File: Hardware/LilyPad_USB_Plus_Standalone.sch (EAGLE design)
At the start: 72 parts, among them J1 SEWTAP_LONG-2SIDE, J10 SEWTAP_LONG-2SIDE, J11 SEWTAP_LONG-2SIDE, J12 SEWTAP_LONG-2SIDE, J13 SEWTAP_LONG-2SIDE, J14 SEWTAP_LONG-2SIDE, J15 AMP FCI 10103594-0001LF, J2 SEWTAP_LONG-2SIDE, J3 SEWTAP_LONG-2SIDE, J4 SEWTAP_LONG-2SIDE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

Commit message: Cleaned up some things
Ready for proto review
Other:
- note added: "Revised by: Elias Santistevan"
- note added: "v01"
- note removed: "v10"
- moved on the sheet: TP5, TP6
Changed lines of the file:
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@@
 <text x="220.98" y="151.13" size="1.27" layer="97">MIC5219 BYPASS</text>
 <text x="171.45" y="11.43" size="2.54" layer="94">Marshall Taylor</text>
-<text x="238.252" y="7.112" size="2.54" layer="94">v10</text>
+<text x="238.252" y="7.112" size="2.54" layer="94">v01</text>
 <text x="149.86" y="38.1" size="2.54" layer="94">LilyPad concept and shapes by:
 L. Buechley and N. Seidle</text>
@@
 <text x="5.08" y="5.08" size="2.032" layer="97" font="vector">Supply 5.0V from USB, or
 3.3-4.2V on battery connector.</text>
+<text x="148.844" y="7.112" size="2.54" layer="94">Revised by: Elias Santistevan</text>
 </plain>
 <instances>
@@
 <instance part="GND26" gate="1" x="172.72" y="144.78"/>
 <instance part="U$1" gate="G$1" x="220.98" y="38.1"/>
-<instance part="LOGO6" gate="G$1" x="233.68" y="53.34"/>
+<instance part="LOGO6" gate="G$1" x="233.68" y="55.88"/>
 <instance part="D10" gate="G1" x="157.48" y="157.48" smashed="yes">
 <attribute name="NAME" x="149.86" y="162.8775" size="1.778" layer="95" font="vector"/>
 <attribute name="VALUE" x="139.7" y="152.0825" size="1.778" layer="95" font="vector" align="top-left"/>
 </instance>
-<instance part="TP5" gate="G$1" x="167.64" y="58.42" rot="R180"/>
-<instance part="TP6" gate="G$1" x="167.64" y="68.58" rot="R180"/>
-<instance part="GND28" gate="1" x="172.72" y="53.34"/>
-<instance part="P+9" gate="G$1" x="172.72" y="73.66"/>
+<instance part="TP5" gate="G$1" x="170.18" y="58.42" rot="R180"/>
+<instance part="TP6" gate="G$1" x="170.18" y="68.58" rot="R180"/>
+<instance part="GND28" gate="1" x="175.26" y="53.34"/>
+<instance part="P+9" gate="G$1" x="175.26" y="73.66"/>
 <instance part="TP7" gate="G$1" x="93.98" y="48.26" rot="R90"/>
 <instance part="TP8" gate="G$1" x="109.22" y="22.86"/>
-<instance part="LOGO1" gate="G$1" x="88.9" y="-2.54"/>
+<instance part="LOGO1" gate="G$1" x="90.932" y="-2.032"/>
 </instances>
 <busses>
@@
 <pinref part="TP5" gate="G$1" pin="1"/>
 <pinref part="GND28" gate="1" pin="GND"/>
-<wire x1="167.64" y1="58.42" x2="172.72" y2="58.42" width="0.1524" layer="91"/>
-<wire x1="172.72" y1="58.42" x2="172.72" y2="55.88" width="0.1524" layer="91"/>
+<wire x1="170.18" y1="58.42" x2="175.26" y2="58.42" width="0.1524" layer="91"/>
+<wire x1="175.26" y1="58.42" x2="175.26" y2="55.88" width="0.1524" layer="91"/>
 </segment>
 </net>
@@
 <pinref part="TP6" gate="G$1" pin="1"/>
 <pinref part="P+9" gate="G$1" pin="3.3V"/>
-<wire x1="167.64" y1="68.58" x2="172.72" y2="68.58" width="0.1524" layer="91"/>
-<wire x1="172.72" y1="68.58" x2="172.72" y2="73.66" width="0.1524" layer="91"/>
-</segment>
-</net>
+<wire x1="170.18" y1="68.58" x2="175.26" y2="68.58" width="0.1524" layer="91"/>
+<wire x1="175.26" y1="68.58" x2="175.26" y2="73.66" width="0.1524" layer="91"/>
+</segment>
+</net>

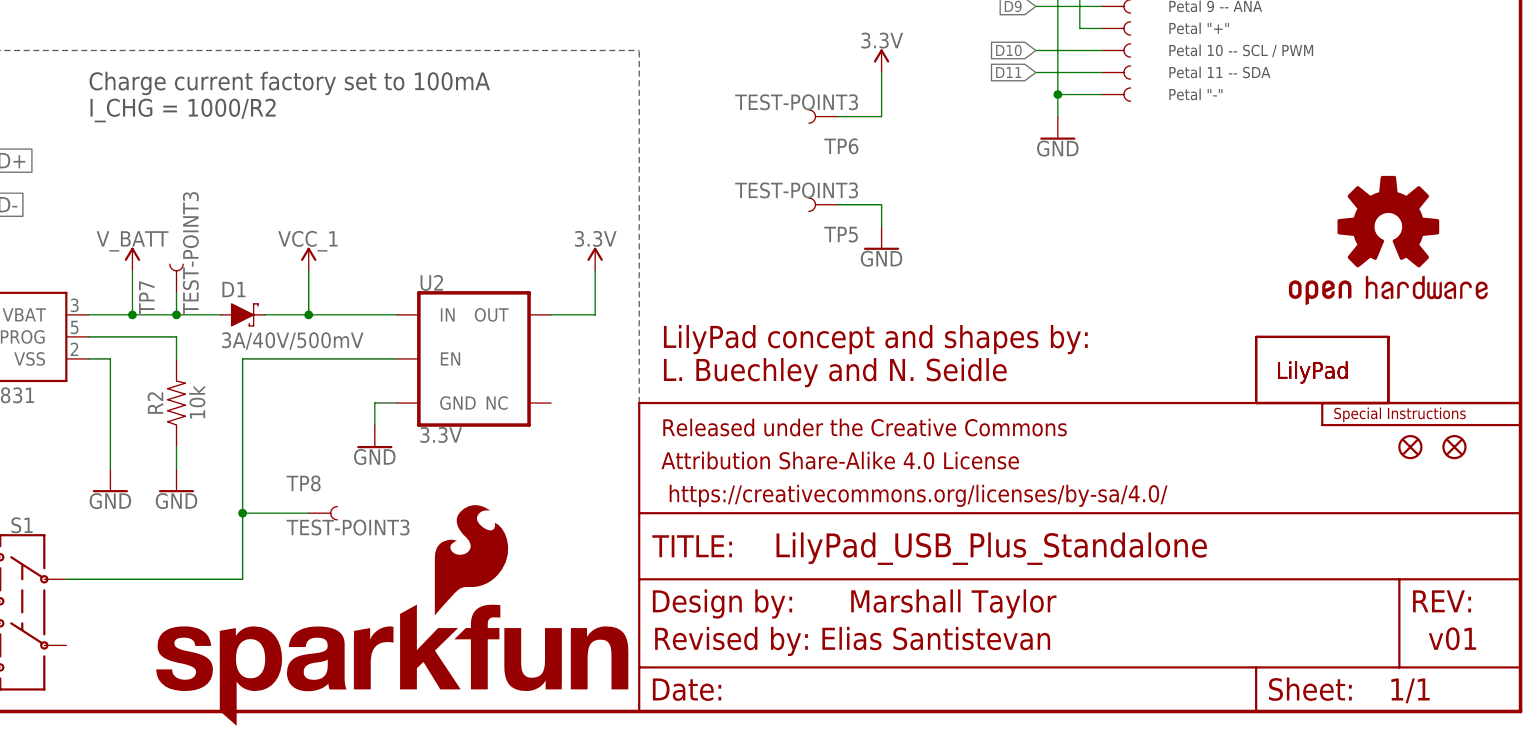
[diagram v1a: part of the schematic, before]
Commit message: Issues found from my double check
Fiducials on underside placed, Sparkfun name on board changed to flame according to Lilypad design rules.
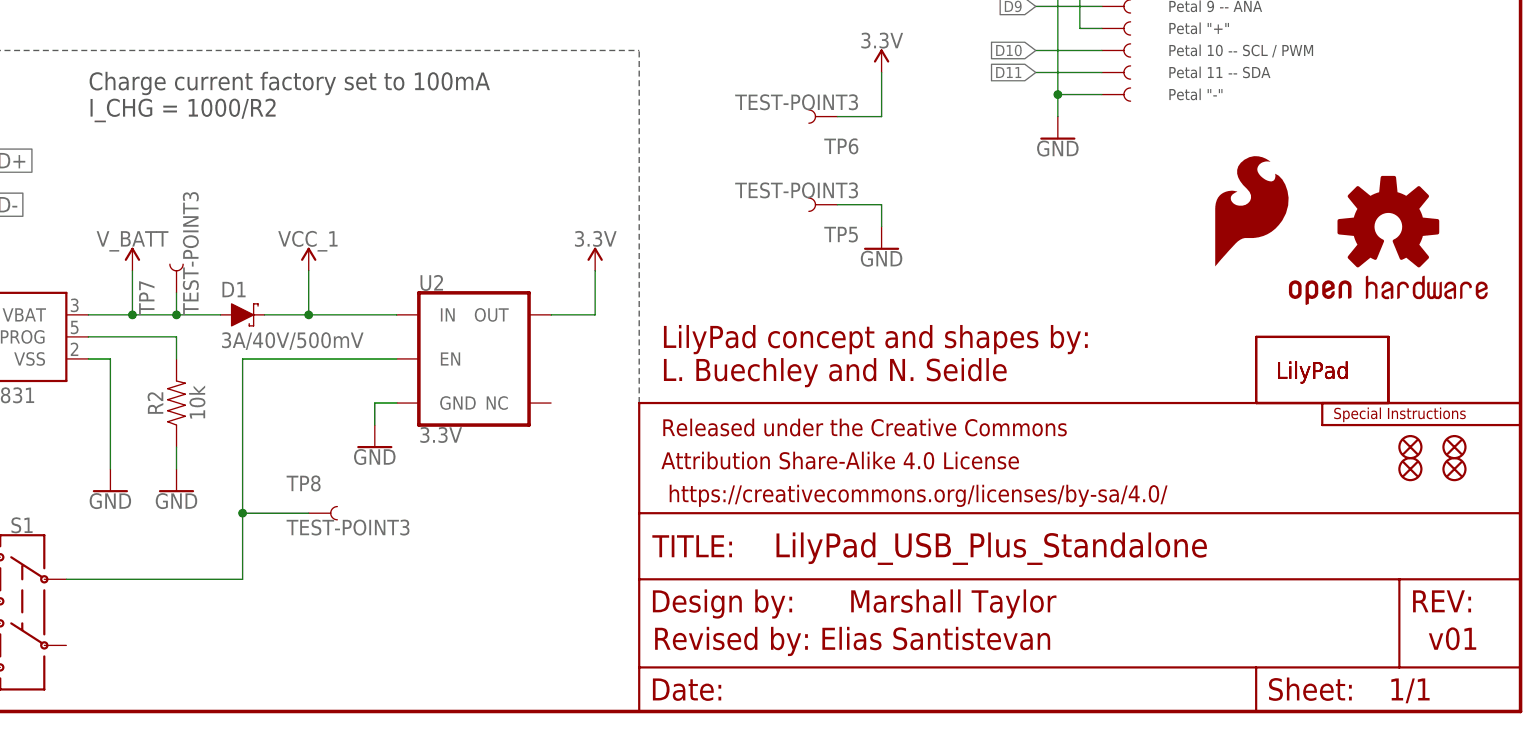
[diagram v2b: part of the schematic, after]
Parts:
- added JP1, JP4: FIDUCIALUFIDUCIAL, SparkFun:FIDUCIALUFIDUCIAL
- LOGO1: value SFE_LOGO_NAME_FLAME.1_INCH -> SFE_LOGO_FLAME.2_INCH; device SparkFun-Aesthetics:SFE_LOGO_NAME_FLAME.1_INCH -> SparkFun-Aesthetics:SFE_LOGO_FLAME.2_INCH
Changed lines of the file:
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@@
 <part name="TP7" library="SparkFun-Connectors" deviceset="TEST-POINT" device="3"/>
 <part name="TP8" library="SparkFun-Connectors" deviceset="TEST-POINT" device="3"/>
-<part name="LOGO1" library="SparkFun-Aesthetics" deviceset="SFE_LOGO_NAME_FLAME" device=".1_INCH"/>
+<part name="JP1" library="SparkFun" deviceset="FIDUCIAL" device="UFIDUCIAL"/>
+<part name="JP4" library="SparkFun" deviceset="FIDUCIAL" device="UFIDUCIAL"/>
+<part name="LOGO1" library="SparkFun-Aesthetics" deviceset="SFE_LOGO_FLAME" device=".2_INCH"/>
 </parts>
 <sheets>
@@
 <instance part="TP7" gate="G$1" x="93.98" y="48.26" rot="R90"/>
 <instance part="TP8" gate="G$1" x="109.22" y="22.86"/>
-<instance part="LOGO1" gate="G$1" x="90.932" y="-2.032"/>
+<instance part="JP1" gate="G$1" x="236.22" y="27.94"/>
+<instance part="JP4" gate="G$1" x="241.3" y="27.94"/>
+<instance part="LOGO1" gate="G$1" x="213.36" y="50.8"/>
 </instances>
 <busses>
